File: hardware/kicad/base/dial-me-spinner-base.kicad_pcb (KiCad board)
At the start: 2 copper layers, 57.6 x 46 mm, 25 parts, among them J1 TYPE-C-31-M-12, J2 BATT, J3 LINK, Q1 BSS138DW, SW1 TS-1187A, U1 BQ25180YBGR, U2 USBLC6-2SC6

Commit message: WIP: docs/mechanical/board updates in progress
Co-Authored-By: Claude Opus 5.5 <noreply@anthropic.com>
Claude-Session: https://claude.ai/code/session_01P3cqdBhxLcWY3sGUVf9LAJ
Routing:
- net GND: track 0.95 -> 182.0 mm
- net VBUS: track 0.80 -> 97.9 mm, vias 0 -> 5
- net VBAT: track 1.34 -> 45.3 mm, vias 0 -> 2
- net VSYS: track 1.40 -> 44.4 mm
- net /Base board/SW_GATE: track 0.00 -> 16.7 mm, vias 0 -> 2
- net /Base board/SW_HI: track 0.00 -> 3.17 mm
- net /Base board/CHG_TSMR: track 0.80 -> 3.33 mm
- net /Base board/USB_DP: track 4.35 -> 6.63 mm
- net /Base board/USB_DM: track 6.35 -> 8.63 mm

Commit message: WIP: routing, SPICE tests and docs in progress
Co-Authored-By: Claude Opus 5.5 <noreply@anthropic.com>
Claude-Session: https://claude.ai/code/session_01P3cqdBhxLcWY3sGUVf9LAJ
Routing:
- net /Base board/USB_DM: track 8.63 -> 66.3 mm, vias 0 -> 3
- net /Base board/USB_DP: track 6.63 -> 20.5 mm
- net /Base board/SW_HI: track 3.17 -> 11.7 mm
- net /Base board/USB_CC1: track 0.00 -> 7.66 mm, vias 0 -> 2
- net /Base board/USB_CC2: track 0.00 -> 2.43 mm

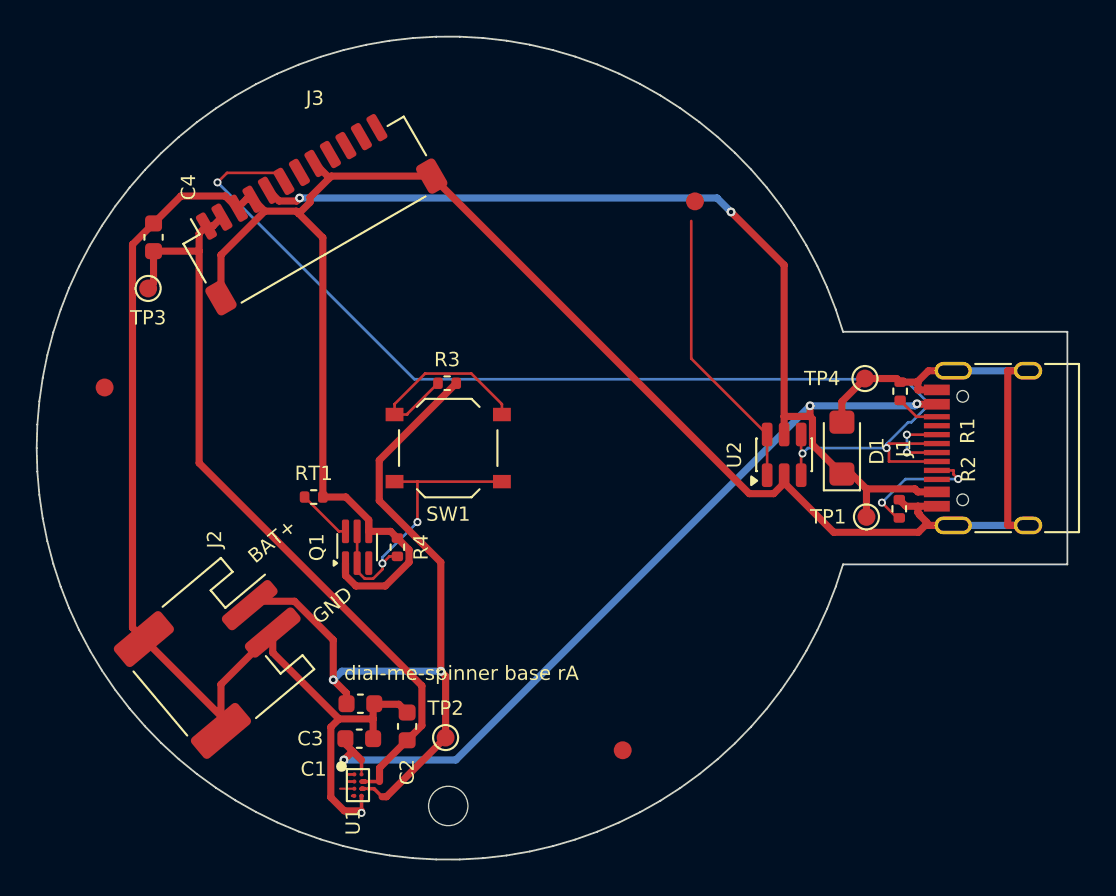
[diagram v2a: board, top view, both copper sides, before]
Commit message: Mechanical fit: SH battery connector, module u.FL outward, J1 out of the hub zone
- base J2: JST SH 4-pin side-entry (PH was too tall under the pressed rotor web)
- main: MDBT50Q inner end r >= 8.8 with u.FL facing out; J1 at r 19.5; top r <= 4.6
  kept for the spindle nut; low-profile-only actuator corridor on the bottom
- placer: keep-outs can exempt footprints (low-profile parts)
- enclosure model: coax and battery-lead paths follow the new placement; clash check
  shows only the intended contacts
- docs synced to the earlier late-change list; SPEC updated

Co-Authored-By: Claude Opus 5.5 <noreply@anthropic.com>
Claude-Session: https://claude.ai/code/session_01P3cqdBhxLcWY3sGUVf9LAJ
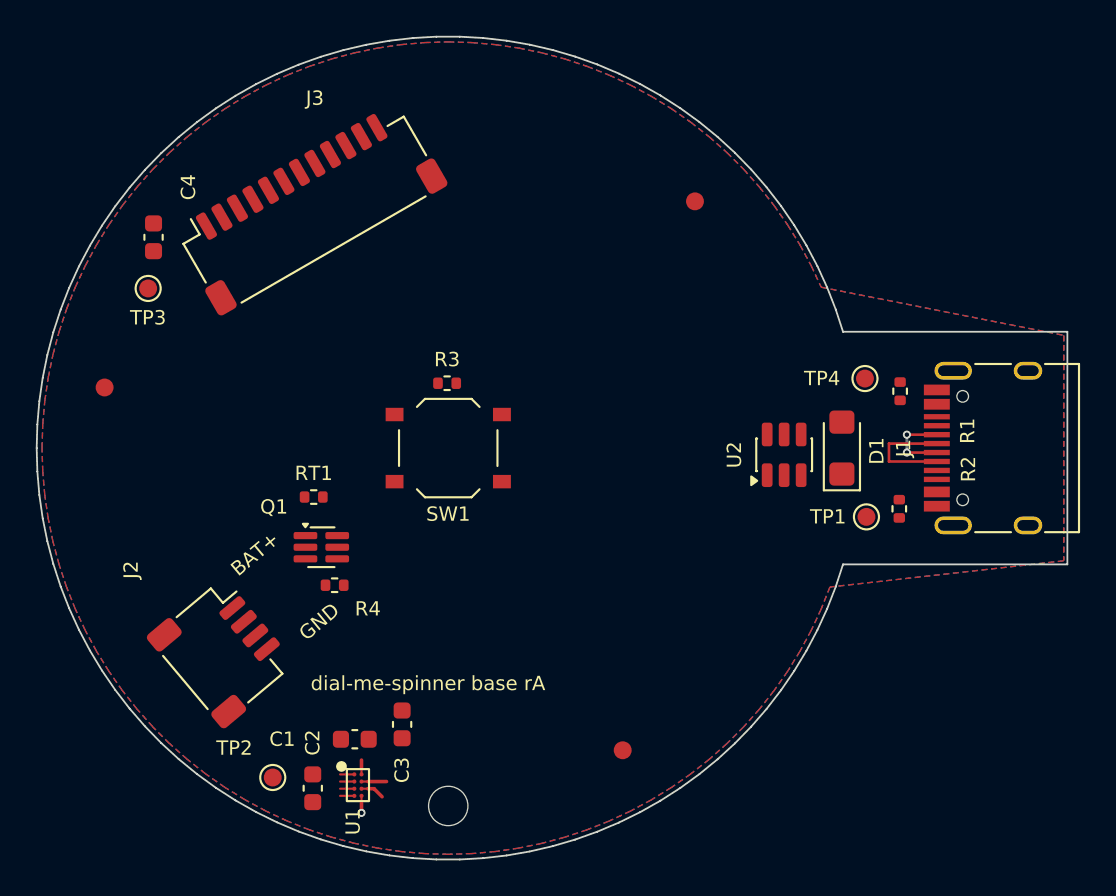
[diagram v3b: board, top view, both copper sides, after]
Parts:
- J2: footprint Connector_JST:JST_PH_S2B-PH-SM4-TB_1x02-1MP_P2.00mm_Horizontal -> Connector_JST:JST_SH_SM04B-SRSS-TB_1x04-1MP_P1.00mm_Horizontal
- moved TP2 9.91 mm to (90.2, 118.4)
- moved C2 6.31 mm to (92.4, 119.0)
- moved R4 4.10 mm to (93.7, 107.7), turned to 0 degrees
- moved C3 2.60 mm to (97.4, 115.4), turned to 90 degrees
- moved Q1 2.00 mm to (92.9, 105.5), turned to 0 degrees
- moved C1 0.25 mm to (94.8, 116.3)
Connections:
- J2 pad 2: GND -> VBAT
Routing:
- net GND: track 182.2 -> 0.95 mm
- net VBUS: track 97.9 -> 0.80 mm, vias 5 -> 0
- net /Base board/USB_DM: track 66.3 -> 6.35 mm, vias 3 -> 0
- net VBAT: track 45.4 -> 1.34 mm, vias 2 -> 0
- net VSYS: track 44.6 -> 1.40 mm
- net /Base board/SW_GATE: track 16.7 -> 0.00 mm, vias 2 -> 0
- net /Base board/USB_DP: track 20.5 -> 4.35 mm
- net /Base board/SW_HI: track 11.7 -> 0.00 mm
- net /Base board/USB_CC1: track 7.66 -> 0.00 mm, vias 2 -> 0
- net /Base board/CHG_TSMR: track 3.40 -> 0.80 mm
- net /Base board/USB_CC2: track 2.43 -> 0.00 mm
- added copper zone on B.Cu, net GND
- added copper zone on F.Cu, net GND

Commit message: WIP: SPICE tests and boards in progress
Co-Authored-By: Claude Opus 5.5 <noreply@anthropic.com>
Claude-Session: https://claude.ai/code/session_01P3cqdBhxLcWY3sGUVf9LAJ
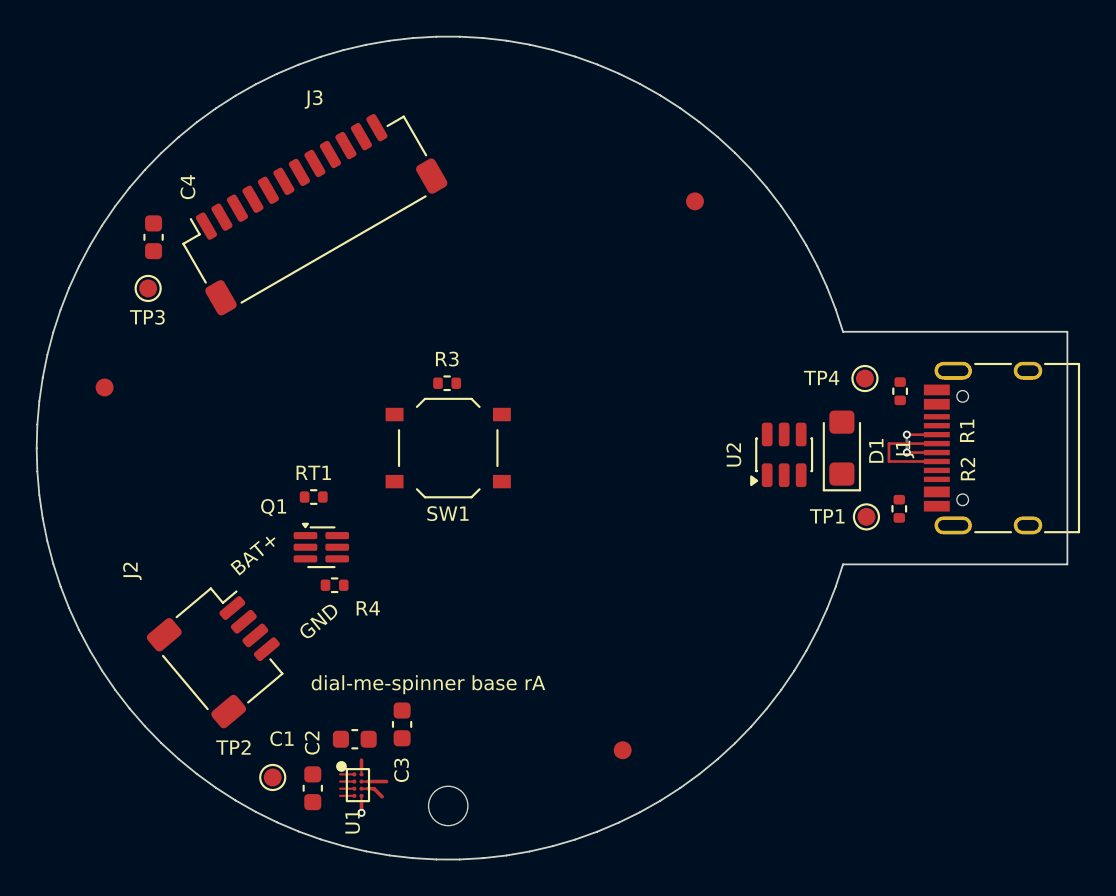
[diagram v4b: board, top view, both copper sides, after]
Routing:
- removed copper zone on B.Cu, net GND
- removed copper zone on F.Cu, net GND
